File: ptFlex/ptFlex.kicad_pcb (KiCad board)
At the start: 2 copper layers, 50.1 x 88.2 mm, 72 parts, among them J1 Barrel_Jack_Switch, J2 Programming, J3 Qwiic, J4 6 Pin Male Header, Q1 MMBT3904, Q2 MMBT3904, Q3 DMP2004K-7, Q4 BSS138, Q5 BSS138, U1 LM1086-5.0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

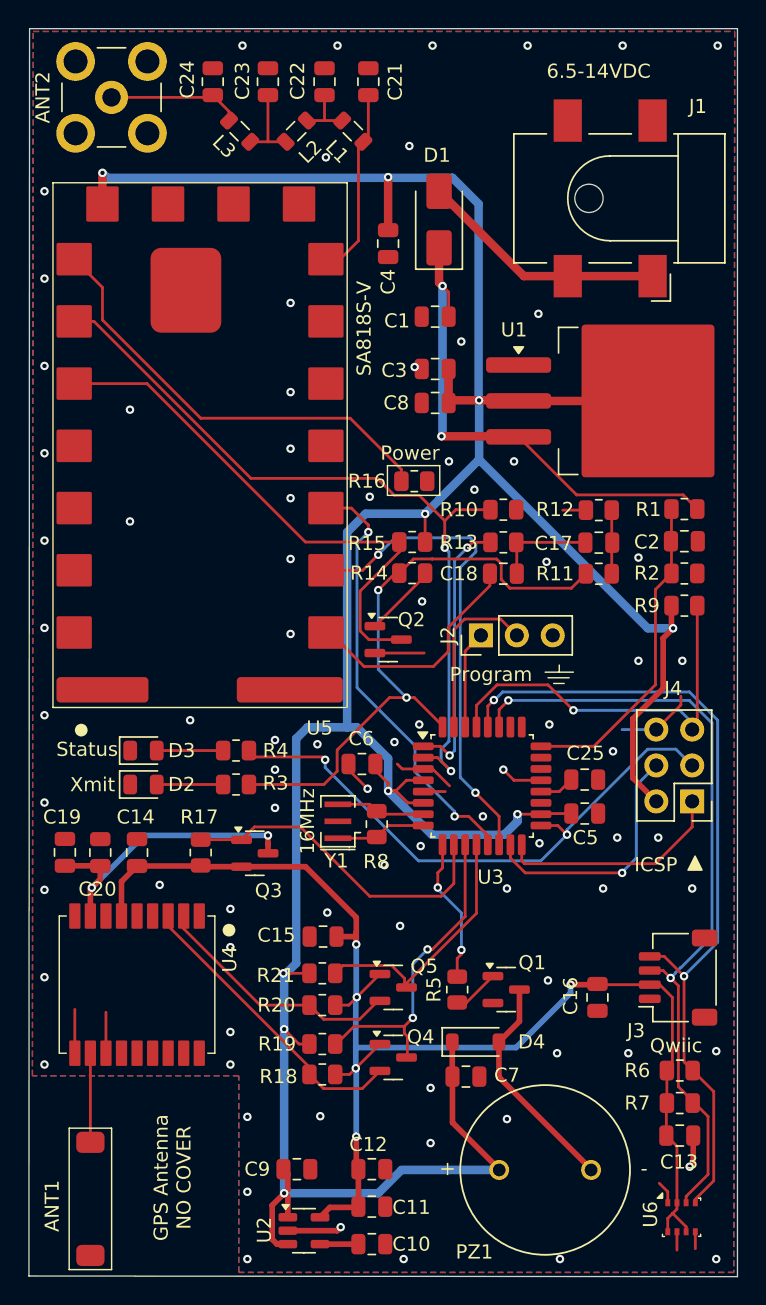
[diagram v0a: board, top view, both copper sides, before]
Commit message: Finalizing PCB v2.0.2. Including some minor tweaks to the firmware as well.
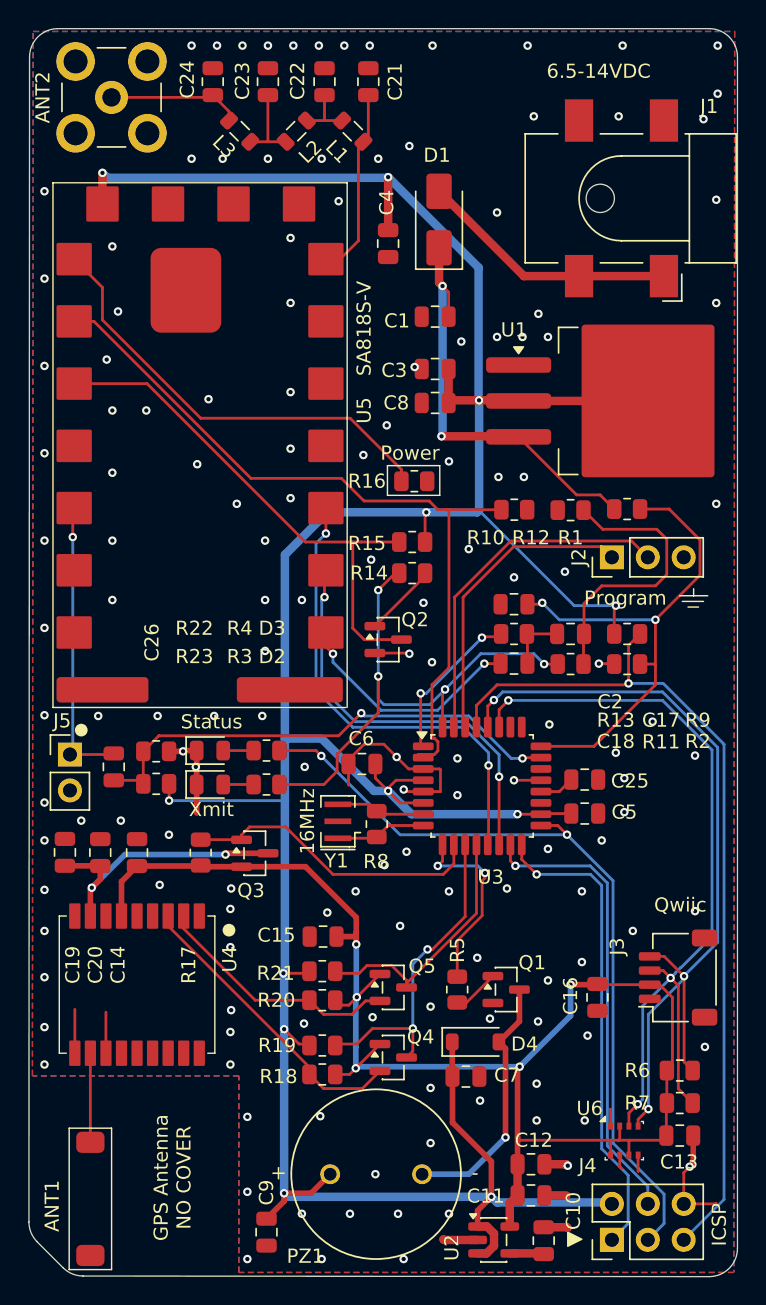
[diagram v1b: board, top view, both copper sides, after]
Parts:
- added C26: 1uF, Capacitor_SMD:C_0805_2012Metric, F.Cu at (122.3, 109.8)
- added J5: Rx Aud, Connector_PinHeader_2.54mm:PinHeader_1x02_P2.54mm_Vertical, F.Cu at (119.2, 108.9)
- added R22: 10k, Resistor_SMD:R_0805_2012Metric, F.Cu at (125.3, 111.0)
- added R23: 10k, Resistor_SMD:R_0805_2012Metric, F.Cu at (125.3, 108.7)
- moved J4 31.5 mm to (157.5, 143.2), turned to 90 degrees
- moved U2 13.4 mm to (149.2, 143.2)
- moved C2 12.8 mm to (150.6, 98.3), turned to 180 degrees
- moved C10 12.2 mm to (152.7, 143.3), turned to 90 degrees
- moved PZ1 12.0 mm to (140.8, 138.6)
- moved C11 11.3 mm to (151.8, 140.1)
- moved C12 11.3 mm to (151.8, 137.9)
- moved J2 10.8 mm to (157.5, 95.0)
- moved R2 7.58 mm to (158.6, 102.5), turned to 0 degrees
- moved U6 6.76 mm to (158.4, 136.2)
- moved C17 6.76 mm to (154.6, 100.4)
- moved R11 6.69 mm to (154.6, 102.5)
- moved R13 6.52 mm to (150.6, 100.4)
- moved C18 6.41 mm to (150.6, 102.5)
- moved C9 4.94 mm to (133.1, 142.7), turned to -90 degrees
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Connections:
- U3 pad 23: unconnected-(U3-PC0-Pad23) -> XMIT-RX-AUDIO
- U5 pad 3: unconnected-(U5-AF-OUT-Pad3) -> Net-(J5-Pin_1)
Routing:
- net XMIT-RX-AUDIO: track 0.00 -> 35.1 mm, vias 0 -> 2
- net RESET: track 28.2 -> 61.4 mm
- net Net-(J5-Pin_1): track 0.00 -> 20.7 mm, vias 0 -> 1
- net MISO: track 16.1 -> 33.8 mm, vias 0 -> 1
- net SCK: track 40.9 -> 56.8 mm
- net Net-(C17-Pad2): track 4.53 -> 20.2 mm
- net MOSI: track 17.8 -> 32.5 mm
- net BATT-SENSE: track 22.7 -> 37.2 mm, vias 0 -> 2
- net Net-(J2-Pin_1): track 7.14 -> 21.5 mm
- net Net-(J2-Pin_2): track 12.0 -> 24.9 mm
- net GND: track 38.3 -> 50.8 mm, vias 82 -> 149
- net XMIT-TX-AUDIO: track 19.2 -> 11.3 mm
- net Net-(D1-K): track 36.0 -> 30.1 mm
- net XMIT-RX: track 34.7 -> 29.4 mm
- net +3.3V: track 99.0 -> 104.2 mm
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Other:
- outline, holes or cut-outs redrawn
- board text added: "ptFlex Tracker - v2.0.2 Custom Digital Services, LLC www.custom-ds.com"
- board text removed: "ptFlex Tracker - v2.0.1 Custom Digital Services, LLC www.custom-ds.com"

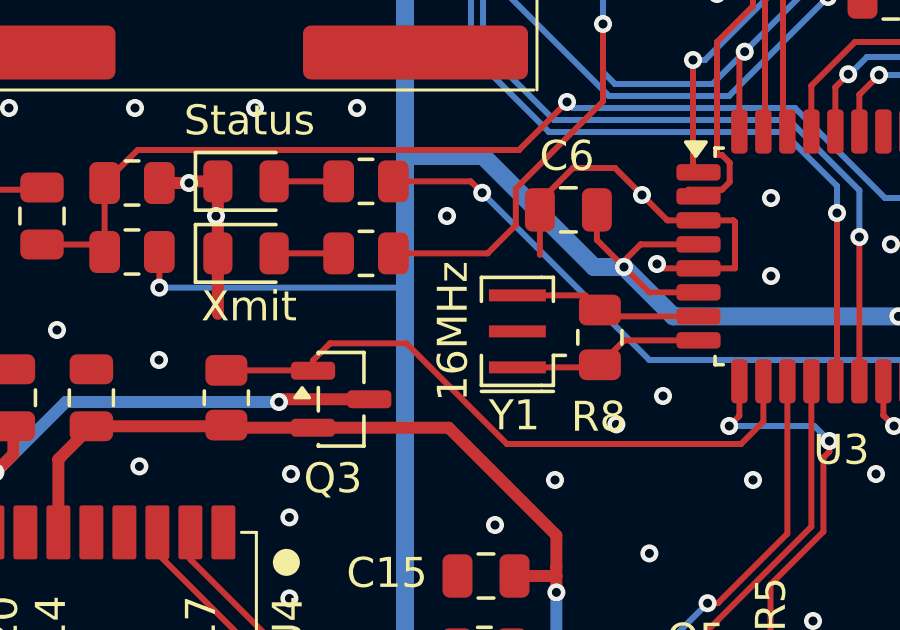
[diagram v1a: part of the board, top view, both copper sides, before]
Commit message: Updated BOM parts
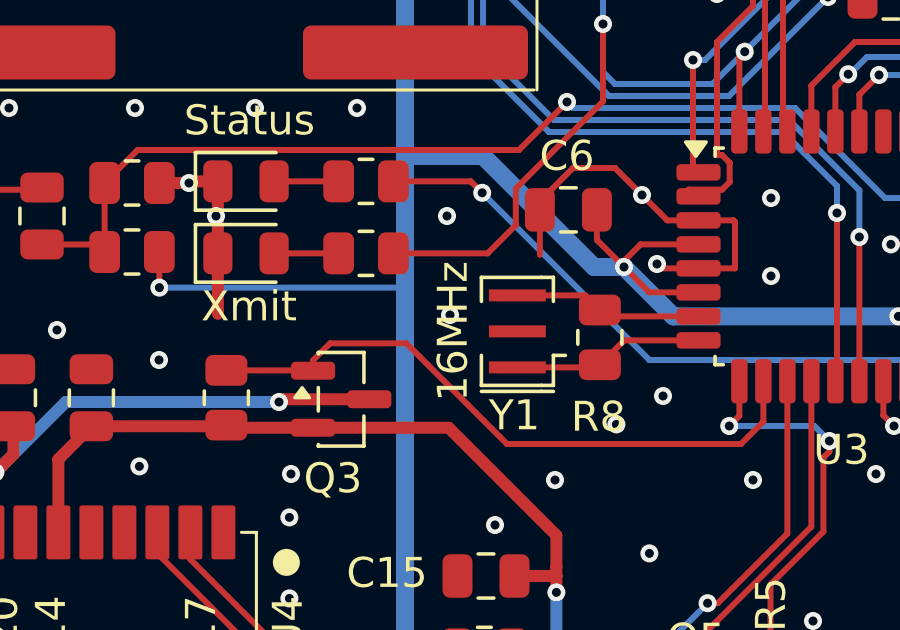
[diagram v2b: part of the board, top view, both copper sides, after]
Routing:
- net GND: vias 149 -> 150
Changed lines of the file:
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@@
+	)
+	(via
+		(at 135.9 113.1)
+		(size 0.6)
+		(drill 0.3)
+		(layers "F.Cu" "B.Cu")
+		(free yes)
+		(net 1)
 	)
 	(via
